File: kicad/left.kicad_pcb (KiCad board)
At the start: 4 copper layers, 127.3 x 89.6 mm, 137 parts, among them Q1 PMF170XP,115, Q2 FS8205A_C2830320, SW1 TS-1088-AR02016, U1 SN74LVC1G17DBVR, U2 E73-2G4M08S1C, U3 SN74LVC1G74DQER, U4 S2B-PH-K-S(LF)(SN), U5 BL8573CS8TR, U6 DW01A_C42380662, U7 LP5024RSMR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

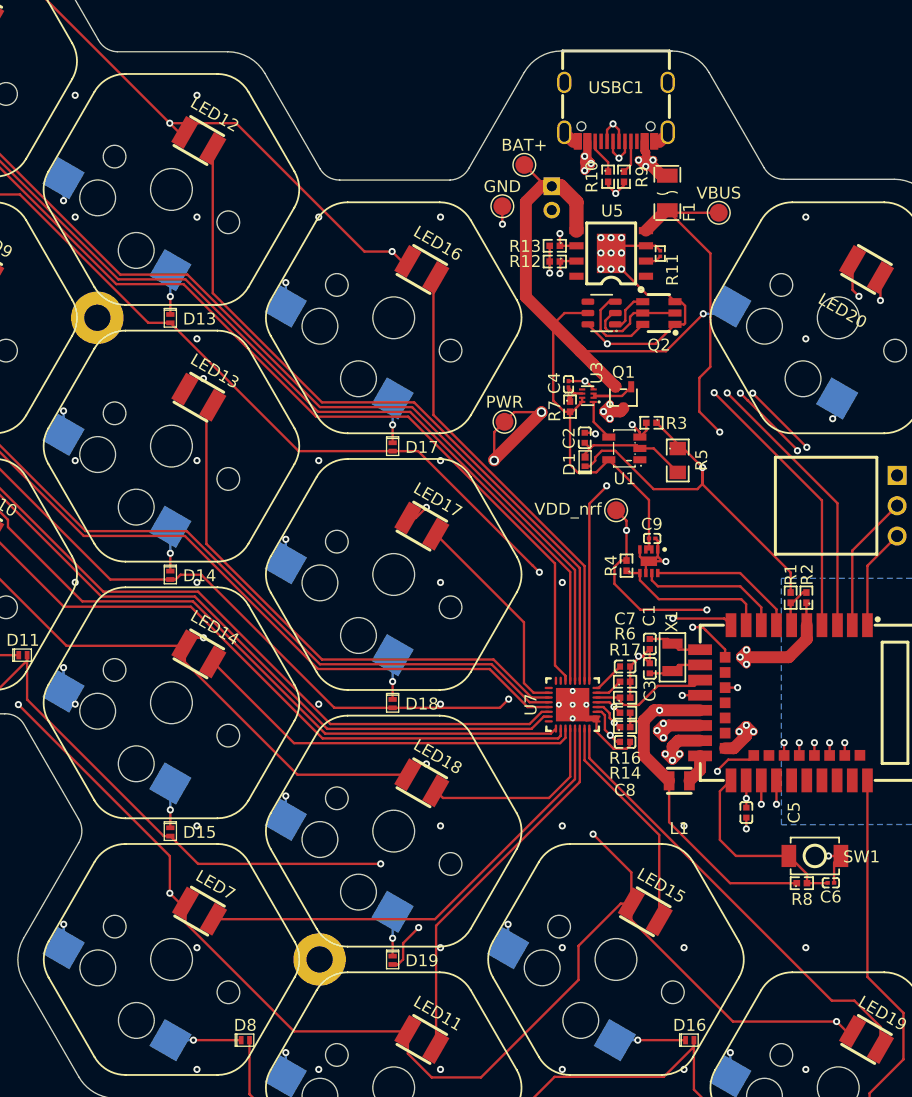
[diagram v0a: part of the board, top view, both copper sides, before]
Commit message: checked most component footprints
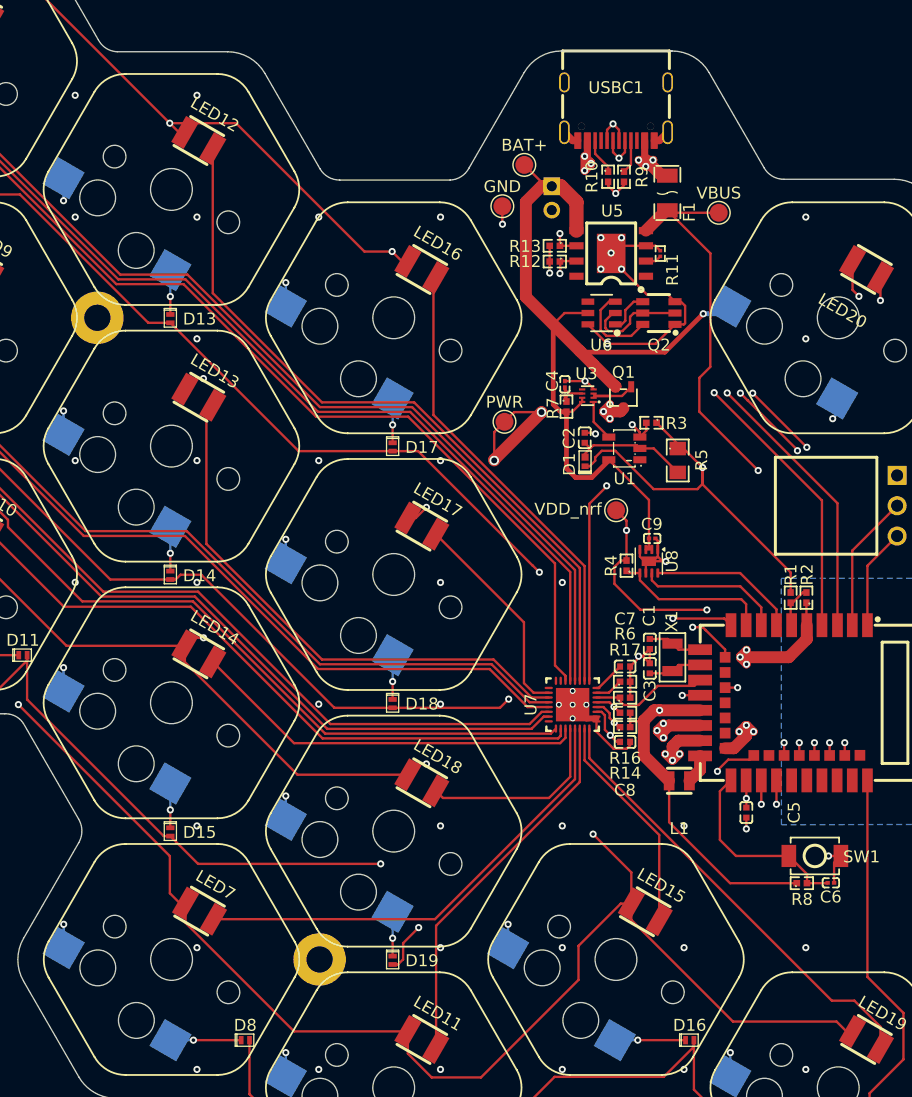
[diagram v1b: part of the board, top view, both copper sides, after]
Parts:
- U6: footprint PCM_JLCPCB:SOT-23-6_L2.9-W1.6-P0.95-LS2.9-BL -> easyeda2kicad:SOT-23-6_L2.9-W1.6-P0.95-LS2.9-BL
- U8: footprint PCM_SparkFun-Semiconductor-Standard:DFN-8_2x2mm_P0.5mm_EP1.2x0.8mm -> Package_DFN_QFN:TDFN-8-1EP_2x2mm_P0.5mm_EP0.8x1.2mm
- moved C4 0.30 mm to (121.7, 54.5)
- moved R7 0.30 mm to (121.8, 56.4)
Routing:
- net /D+: track 79.2 -> 80.8 mm
- net /BAT+: track 75.6 -> 76.7 mm
- net GND: track 85.5 -> 86.5 mm, vias 96 -> 91
- net /STDBY: track 45.2 -> 46.1 mm
- net /PWR: vias 30 -> 28

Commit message: checked and updated all major components
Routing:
- net GND: vias 91 -> 95

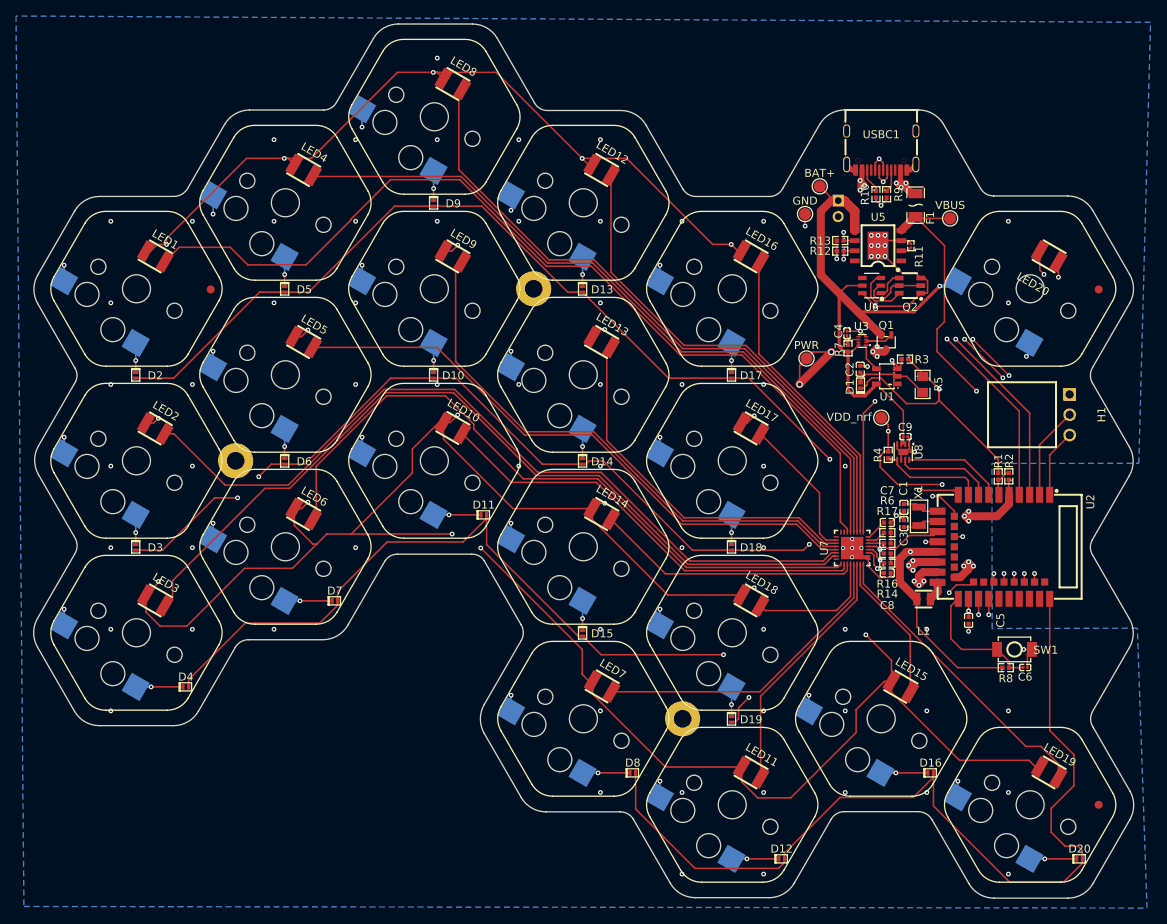
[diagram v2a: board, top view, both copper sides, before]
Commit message: both sides done. changed few components for their basic or more affordable alternaatives.
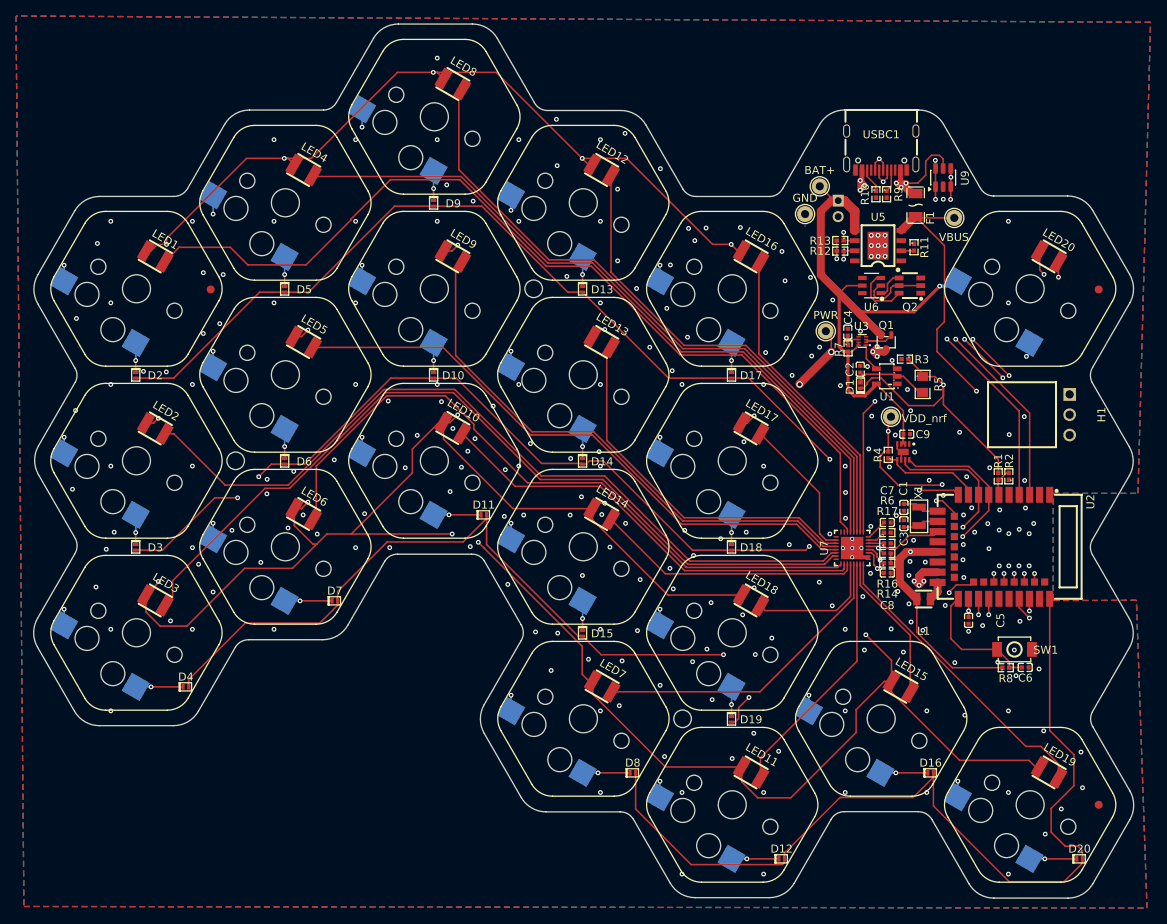
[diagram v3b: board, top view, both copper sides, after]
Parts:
- added U9: USBLC6-2SC6, Package_TO_SOT_SMD:SOT-23-6, F.Cu at (133.7, 35.0)
- BAT+, GND, PWR, VBUS, VDD_nrf: value TestPoint_Pad_D1.5mm -> TestPoint_THTPad_D2.0mm_Drill1.0mm; footprint TestPoint:TestPoint_Pad_D1.5mm -> TestPoint:TestPoint_THTPad_D2.0mm_Drill1.0mm
- C1, C3: value 0402CG120F500NT -> 0402CG120J500NT
- C2: value GRM155Z71A105KE01D -> CL05A105KA5NQNC
- C4, C6, C9: value GRM033C71C104KE14D -> CL05B104KB54PNC; footprint easyeda2kicad:C0201 -> easyeda2kicad:C0402
- C7, C8: value GRM155C71C105KE11D -> CL05A105KA5NQNC
- R1, R17: value RC0402FR-071ML -> 0402WGF1004TCE
- R10, R14, R16, R9: value RC0402FR-075K1L -> 0402WGF5101TCE
- R11: value RC0201FR-07680RL -> RC0402FR-07680RL; footprint easyeda2kicad:R0201 -> easyeda2kicad:R0402
- R12, R13, R4, R7, R8: value RC0402FR-0710KL -> 0402WGF1002TCE
- REF** (x3): value MountingHole_2.2mm_M2_Pad -> MountingHole_2.2mm_M2; footprint MountingHole:MountingHole_2.2mm_M2_Pad -> MountingHole:MountingHole_2.2mm_M2
- U8: footprint Package_DFN_QFN:TDFN-8-1EP_2x2mm_P0.5mm_EP0.8x1.2mm -> PCM_SparkFun-Semiconductor-Standard:DFN-8_2x2mm_P0.5mm_EP1.2x0.8mm
- moved PWR 4.18 mm to (119.0, 54.2)
- moved VDD_nrf 1.22 mm to (127.2, 64.9)
- moved VBUS 0.52 mm to (135.1, 40.1)
- moved R11 0.43 mm to (130.1, 43.7)
- moved C9 0.35 mm to (129.2, 67.1)
- moved C4 0.18 mm to (121.8, 54.3)
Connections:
- net Net-(F1-Pad1) renamed /VBUS_RAW
- U2 pad 1: /SWDIO -> unconnected-(U2-P1.11-Pad1)
- U2 pad 16: /SDA -> unconnected-(U2-P0.08-Pad16)
- U2 pad 17: /SCL -> unconnected-(U2-P1.09-Pad17)
- U2 pad 2: /SWBCLK -> unconnected-(U2-P1.10-Pad2)
- U2 pad 37: unconnected-(U2-SWD-Pad37) -> /SWDIO
- U2 pad 39: unconnected-(U2-SWC-Pad39) -> /SWBCLK
- U2 pad 7: /SDA_BAT -> /SDA
- U2 pad 8: /SCL_BAT -> /SCL
- U8 pad 7: /SCL_BAT -> /SCL
- U8 pad 8: /SDA_BAT -> /SDA
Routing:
- net GND: track 86.5 -> 3.75 mm, vias 95 -> 249
- net /COL5: track 184.1 -> 155.4 mm
- net /SCL: track 9.94 -> 31.2 mm
- net /SWDIO: track 8.50 -> 27.9 mm, vias 0 -> 1
- net /SDA: track 15.5 -> 33.3 mm
- net /SWBCLK: track 11.6 -> 28.1 mm, vias 0 -> 1
- net /SDA_BAT: track 12.5 -> 0.00 mm
- net /SCL_BAT: track 12.2 -> 0.00 mm
- net /VBUS_RAW: track 17.2 -> 25.6 mm
- net /D-: track 78.6 -> 83.2 mm, vias 4 -> 6
- net /LED9: track 70.0 -> 68.3 mm
- net /PWR_BTN: track 47.0 -> 45.6 mm
- net /BAT_ALTR: track 13.3 -> 11.9 mm
- net /BAT+: track 76.7 -> 75.6 mm
- net /VBUS: track 72.8 -> 71.7 mm
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- added copper zone on F.Cu, net GND
- added copper zone on In2.Cu, net GND

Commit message: first panelization... changing parts because of availability
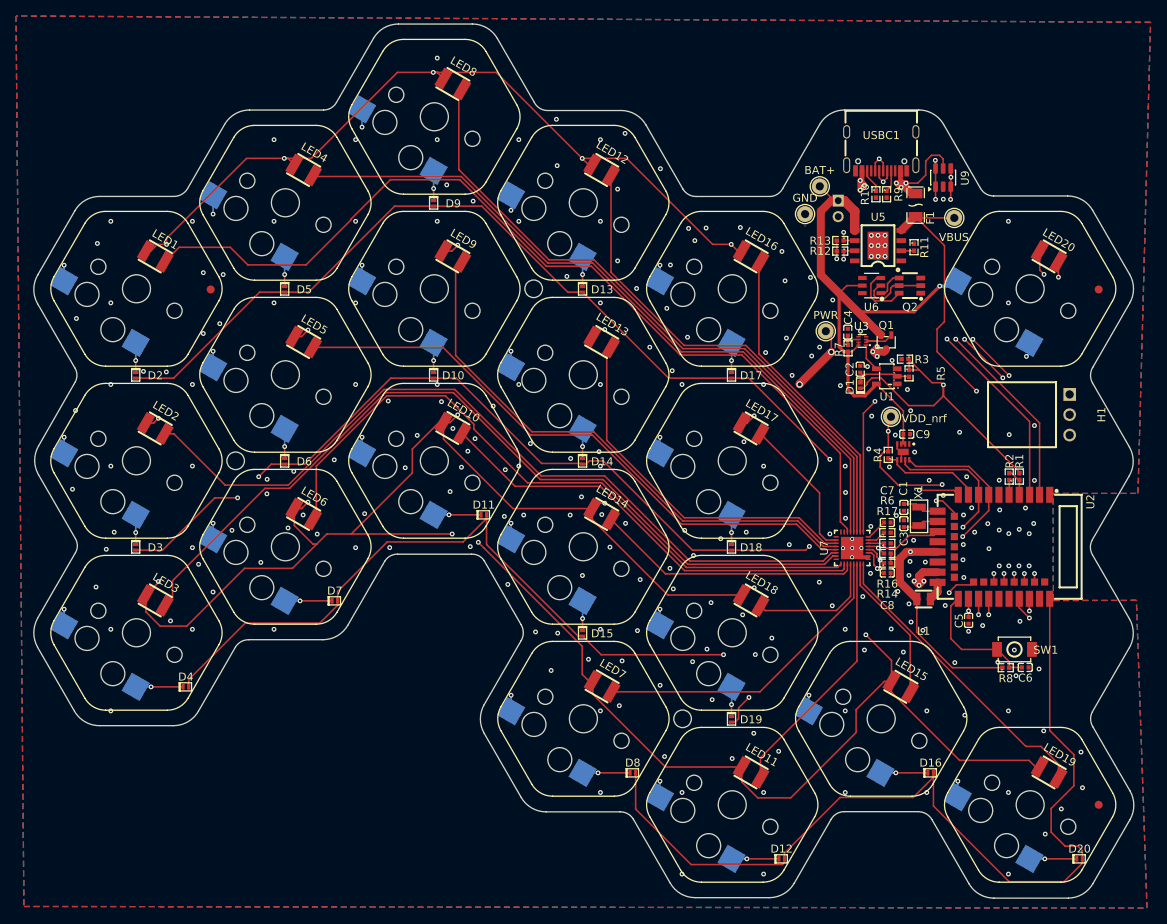
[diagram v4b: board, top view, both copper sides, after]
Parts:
- removed ?, hex_edge (x18): , clipboard:b9cf7df6-7b49-4194-bf11-16aaca528749
- removed Battery?: 3500mAh LiPo, my:3500mAh LiPo
- removed component_safe_space (x3), key_template: , hexcaps:PG1350_hotswap
- R5: value RC0805FR-072M61L -> RTT022614FTH; footprint easyeda2kicad:R0805 -> easyeda2kicad:R0402
- moved R1 2.64 mm to (143.3, 72.4)
- moved R5 2.18 mm to (129.5, 59.5)
- moved USBC1 0.10 mm to (126.0, 31.8)
- moved R2 0.06 mm to (142.0, 72.4)
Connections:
- U2 pad 2: unconnected-(U2-P1.10-Pad2) -> /STDBY
- U2 pad 3: /STDBY -> /CHRG
- U2 pad 4: /CHRG -> /PWR_BTN_PRESS
- U2 pad 6: /PWR_BTN_PRESS -> unconnected-(U2-P1.13-Pad6)
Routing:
- net /PWR_BTN: track 45.6 -> 50.0 mm
- net Net-(U1-A): track 9.93 -> 7.43 mm
- net GND: track 3.75 -> 5.61 mm
- net /CHRG: track 42.6 -> 43.2 mm
- net /STDBY: track 46.1 -> 46.6 mm
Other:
- board size 127.3 x 89.6 mm -> 137.5 x 109.3 mm
